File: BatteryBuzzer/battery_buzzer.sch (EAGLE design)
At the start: 21 parts, among them Q1 IRFML8244, Q2 IRFML8244, Q3 P-CHANNEL-MOSFETSOT23-3, Q4 P-CHANNEL-MOSFETSOT23-3, Q5 P-CHANNEL-MOSFETSOT23-3

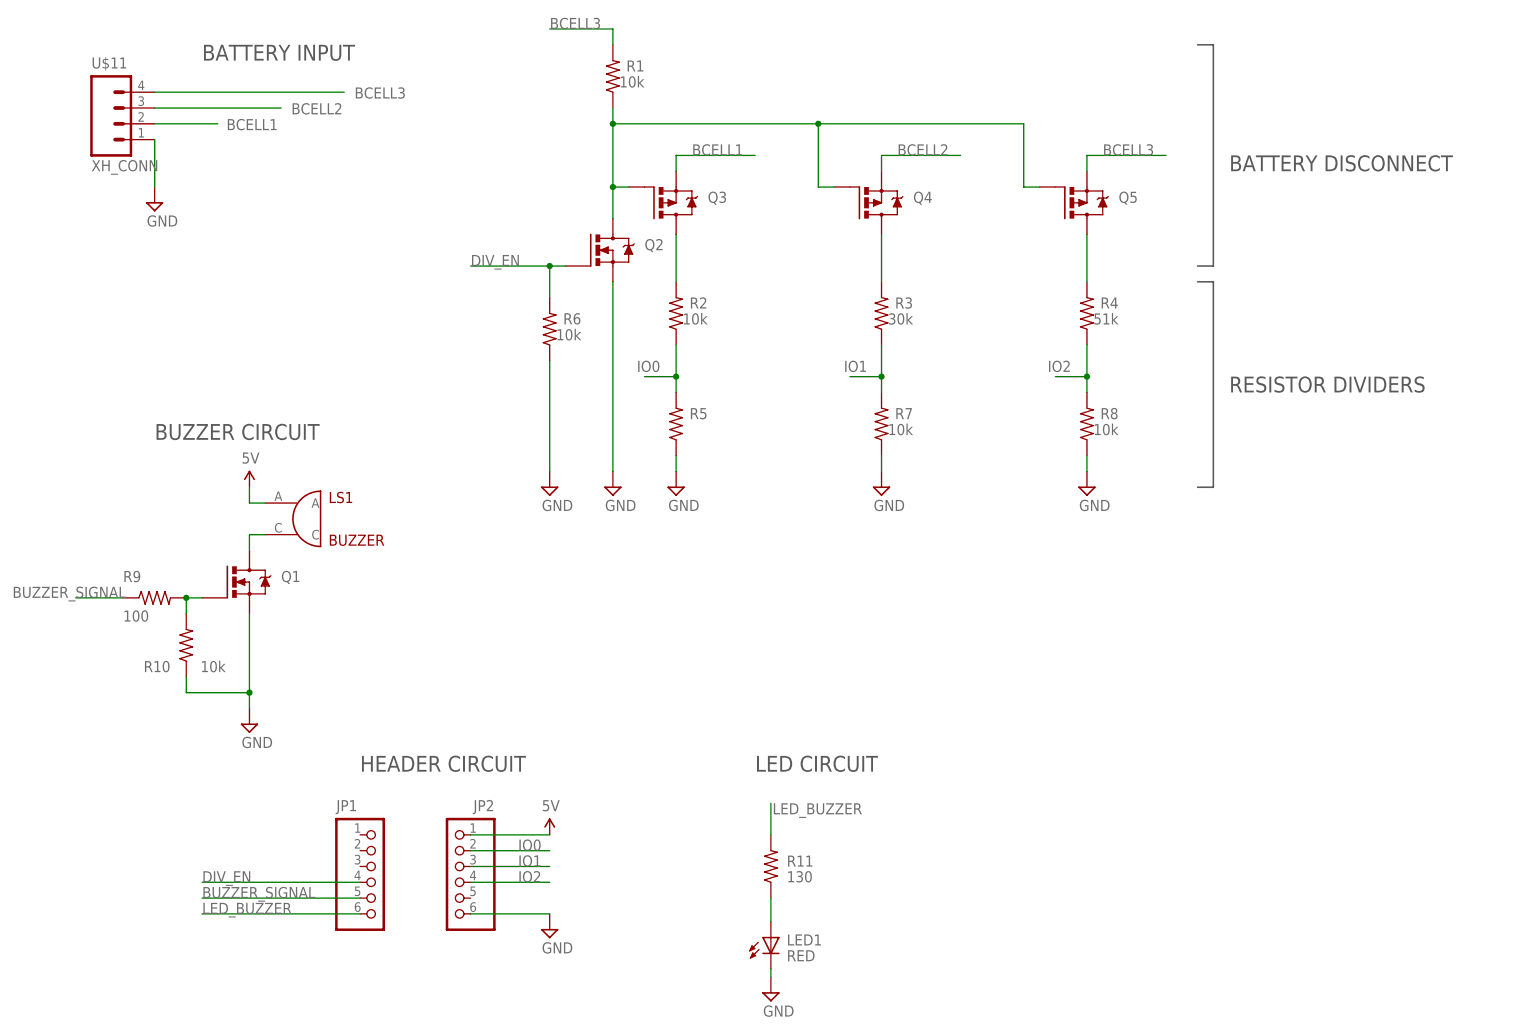
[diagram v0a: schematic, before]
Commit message: bare-bones schematic changes.
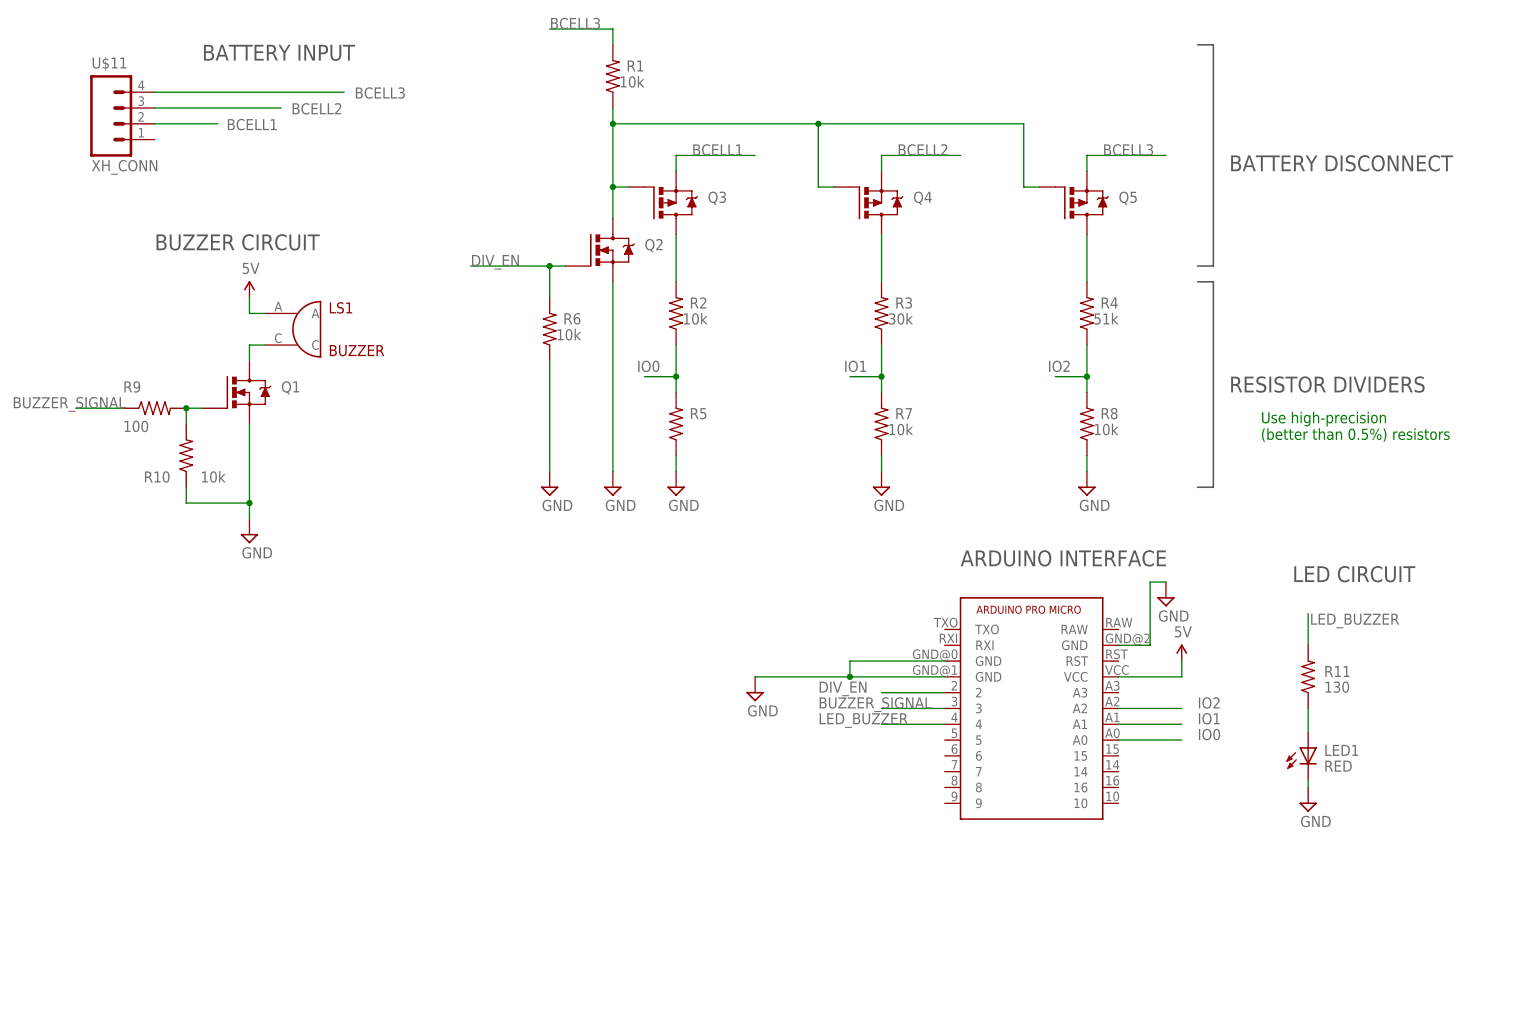
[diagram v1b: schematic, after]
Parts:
- removed JP1, JP2: (no value), pie:PINHD-1X6
- added U$5: ARDUINO_PRO_MICRO, pie:ARDUINO_PRO_MICRO
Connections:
- net 5V: now also U$5.VCC; no longer JP2.1
- net BUZZER_SIGNAL: now also U$5.3; no longer JP1.5
- net DIV_EN: now also U$5.2; no longer JP1.4
- net GND: now also U$5.GND@0, U$5.GND@1, U$5.GND@2; no longer JP2.6, U$11.1
- net IO0: now also U$5.A0; no longer JP2.2
- net IO1: now also U$5.A1; no longer JP2.3
- net IO2: now also U$5.A2; no longer JP2.4
- net LED_BUZZER: now also U$5.4; no longer JP1.6
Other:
- note added: "ARDUINO INTERFACE"
- note added: "Do not connect ground pin on this battery leads unless it has a corrisponding reverse-plugin disconnect: it will short 12V to GND else"
- note added: "Use high-precision (better than 0.5%) resistors"
- note removed: "HEADER CIRCUIT"
- moved on the sheet: LED1, LS1, Q1, R10, R11, R9
